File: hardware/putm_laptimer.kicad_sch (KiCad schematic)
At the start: 44 parts, among them J1 Conn_02x22_Top_Bottom, J10 Conn_01x07, J11 Conn_01x09, J12 Conn_01x01, J13 Conn_01x01, J14 Conn_01x01, J15 Conn_01x01, J16 2601-1103, J2 Conn_02x22_Top_Bottom, J5 2601-3109, J6 Conn_02x05_Odd_Even, J7 2601-1102, J8 2601-3109, J9 Conn_01x07

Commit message: Added part numbers
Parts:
- C1, C10, C3, C4, C5, C6, C7, C8, C9: Link (none) -> https://www.mouser.pl/ProductDetail/KYOCERA-AVX/06035A101KA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; Mouser Part Number (none) -> 581-06035A101K
- D1: Link (none) -> https://eu.mouser.com/ProductDetail/Diodes-Incorporated/DES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
- D2: Link (none) -> https://www.mouser.pl/ProductDetail/Diodes-Incorporated/MBR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
- J1, J2: Link (none) -> https://www.tme.eu/pl/details/zl262-50dg/listwy-i-gniazda-k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; Mouser Part Number (none) -> ZL262-50DG
- J10, J9: Link (none) -> https://www.tme.eu/pl/details/zl262-7sg/listwy-i-gniazda-ko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; Mouser Part Number (none) -> ZL262-7SG
- J11: Link (none) -> https://www.tme.eu/pl/details/zl262-9sg/listwy-i-gniazda-ko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; Mouser Part Number (none) -> ZL262-9SG
- J16, J5, J7, J8: Link (none) -> https://www.wago.com/pl/z%C5%82%C4%85czki-do-p%C5%82ytek-dr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
- J6: Link (none) -> https://www.tme.eu/pl/details/mx-70246-1004/zlacza-pozostal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; Mouser Part Number (none) -> MX-70246-1004
- R1, R11, R13, R15, R17, R19, R5, R7, R9: Link (none) -> https://www.mouser.pl/ProductDetail/Bourns/CR0603-FX-1001EL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; Mouser Part Number (none) -> 652-CR0603FX-1001ELF
- R10, R12, R14, R16, R18, R2, R20, R6, R8: Link (none) -> https://www.mouser.pl/ProductDetail/Bourns/CR0603-FX-1002EL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; Mouser Part Number (none) -> 652-CR0603FX-1002ELF
- R21: Link (none) -> https://www.mouser.pl/ProductDetail/Bourns/CR0603-FX-3300EL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; Mouser Part Number (none) -> 652-CR0603FX-3300ELF

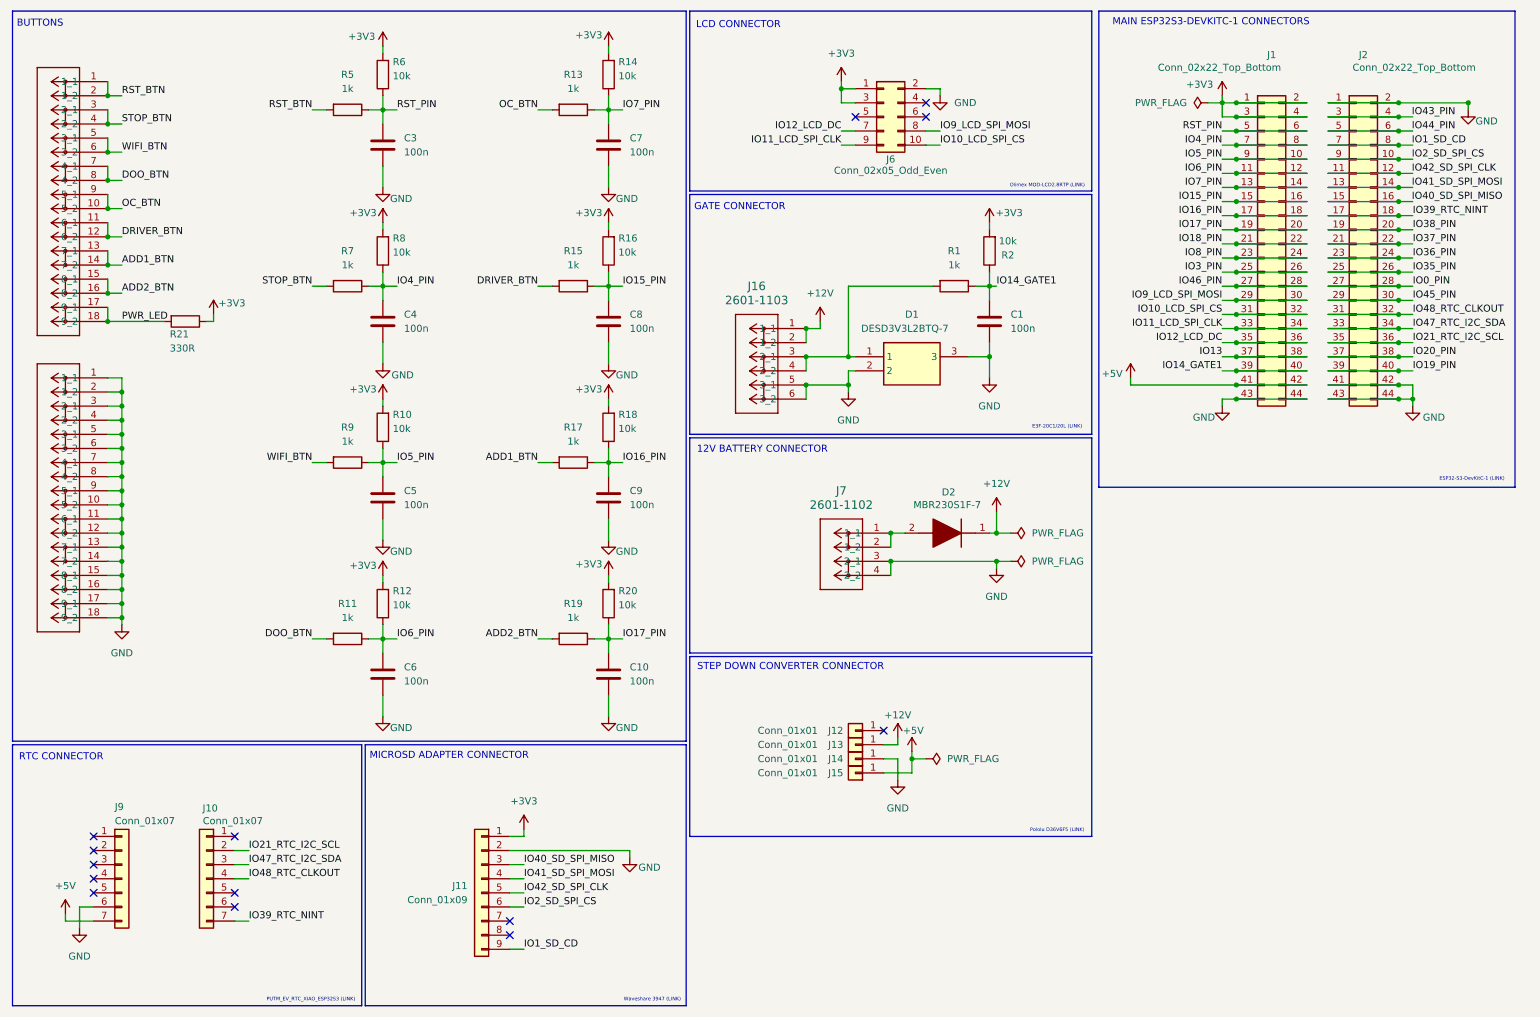
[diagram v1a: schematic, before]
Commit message: Fixed silkscreen text size
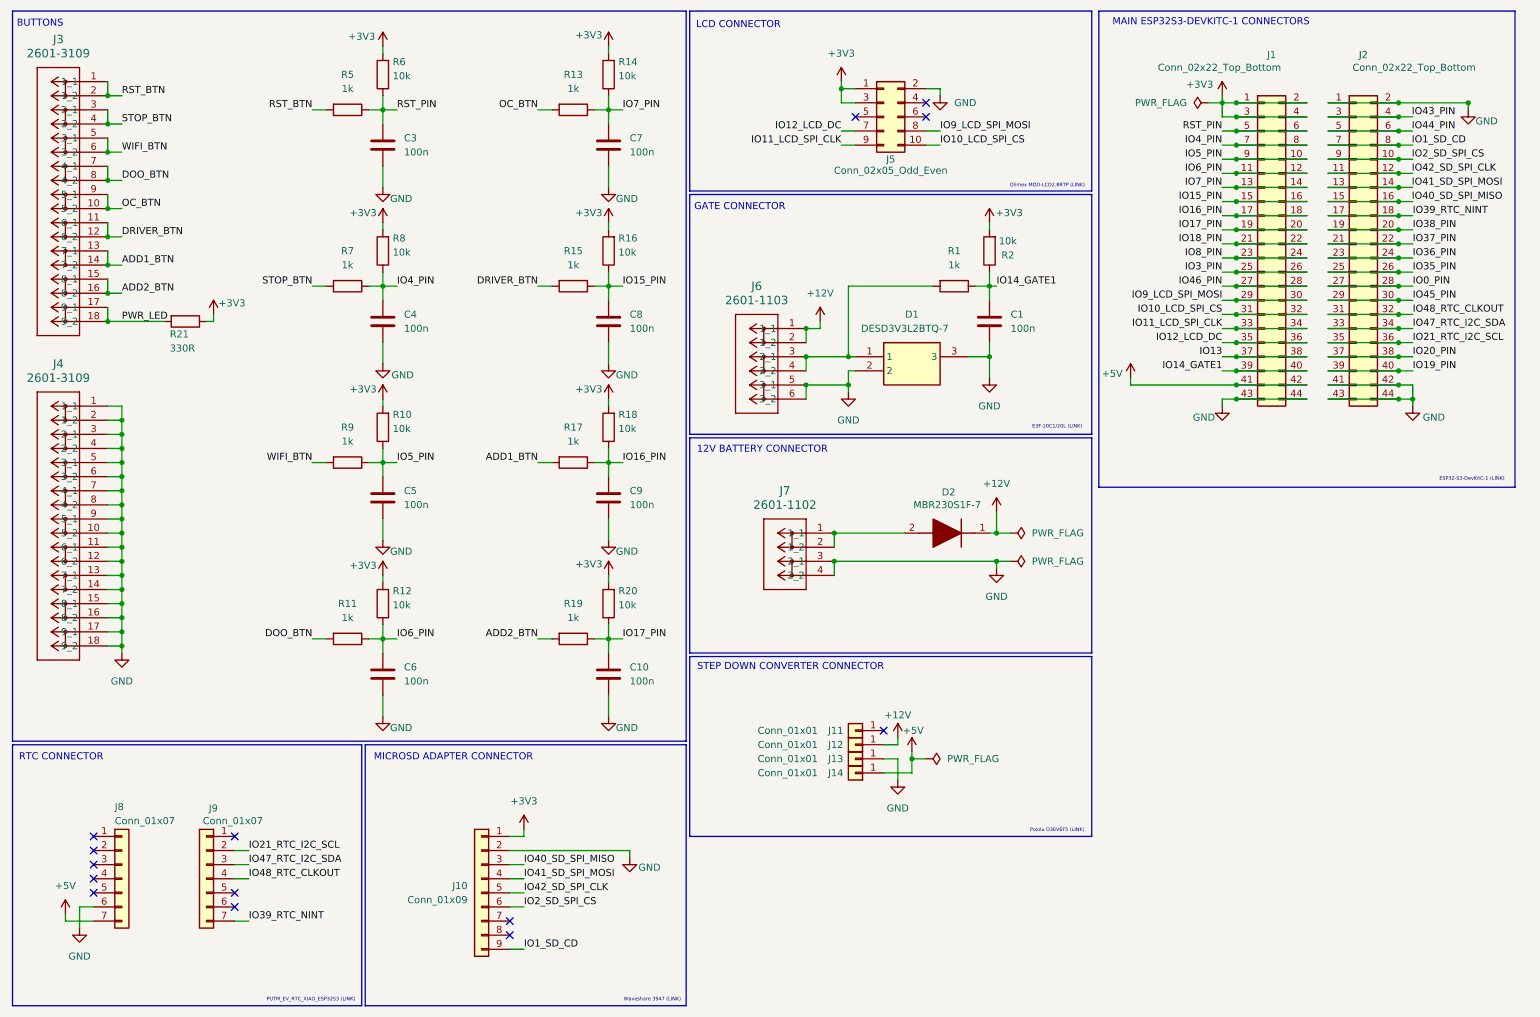
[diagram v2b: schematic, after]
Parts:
- renumbered J11 to J10, J12 to J11, J13 to J12, J14 to J13, J15 to J14, J8 to J3, J5 to J4, J6 to J5, J16 to J6, J9 to J8, J10 to J9
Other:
- moved on the sheet: J7

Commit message: Fixed connector placing
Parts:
- removed J1, J2: Conn_02x22_Top_Bottom, Connector_PinSocket_2.54mm:PinSocket_2x22_P2.54mm_Vertical, symbol Connector_Generic:Conn_02x22_Odd_Even
- added J1, J2, J3, J4: Conn_01x22, Connector_PinSocket_2.54mm:PinSocket_1x22_P2.54mm_Vertical, symbol Connector_Generic:Conn_01x22
- renumbered J8 to J10, J9 to J11, J10 to J12, J11 to J13, J12 to J14, J13 to J15, J14 to J16, J3 to J5, J4 to J6, J5 to J7, J6 to J8, J7 to J9
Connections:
- net +3V3: now also J1.1 (Pin_1), J1.2 (Pin_2), J3.1 (Pin_1), J3.2 (Pin_2)
- net +5V: now also J1.21 (Pin_21), J3.21 (Pin_21)
- net GND: now also J1.22 (Pin_22), J2.1 (Pin_1), J2.21 (Pin_21), J2.22 (Pin_22), J3.22 (Pin_22), J4.1 (Pin_1), J4.21 (Pin_21), J4.22 (Pin_22)
- net IO0_PIN: now also J2.14 (Pin_14), J4.14 (Pin_14)
- net IO10_LCD_SPI_CS: now also J1.16 (Pin_16), J3.16 (Pin_16)
- net IO11_LCD_SPI_CLK: now also J1.17 (Pin_17), J3.17 (Pin_17)
- net IO12_LCD_DC: now also J1.18 (Pin_18), J3.18 (Pin_18)
- net IO13: now also J1.19 (Pin_19), J3.19 (Pin_19)
- net IO14_GATE1: now also J1.20 (Pin_20), J3.20 (Pin_20)
- net IO15_PIN: now also J1.8 (Pin_8), J3.8 (Pin_8)
- net IO16_PIN: now also J1.9 (Pin_9), J3.9 (Pin_9)
- net IO17_PIN: now also J1.10 (Pin_10), J3.10 (Pin_10)
- net IO18_PIN: now also J1.11 (Pin_11), J3.11 (Pin_11)
- net IO19_PIN: now also J2.20 (Pin_20), J4.20 (Pin_20)
- net IO1_SD_CD: now also J2.4 (Pin_4), J4.4 (Pin_4)
- net IO20_PIN: now also J2.19 (Pin_19), J4.19 (Pin_19)
- net IO21_RTC_I2C_SCL: now also J2.18 (Pin_18), J4.18 (Pin_18)
- net IO2_SD_SPI_CS: now also J2.5 (Pin_5), J4.5 (Pin_5)
- net IO35_PIN: now also J2.13 (Pin_13), J4.13 (Pin_13)
- net IO36_PIN: now also J2.12 (Pin_12), J4.12 (Pin_12)
- net IO37_PIN: now also J2.11 (Pin_11), J4.11 (Pin_11)
- net IO38_PIN: now also J2.10 (Pin_10), J4.10 (Pin_10)
- net IO39_RTC_NINT: now also J2.9 (Pin_9), J4.9 (Pin_9)
- net IO3_PIN: now also J1.13 (Pin_13), J3.13 (Pin_13)
- net IO40_SD_SPI_MISO: now also J2.8 (Pin_8), J4.8 (Pin_8)
- net IO41_SD_SPI_MOSI: now also J2.7 (Pin_7), J4.7 (Pin_7)
- net IO42_SD_SPI_CLK: now also J2.6 (Pin_6), J4.6 (Pin_6)
- net IO43_PIN: now also J2.2 (Pin_2), J4.2 (Pin_2)
- net IO44_PIN: now also J2.3 (Pin_3), J4.3 (Pin_3)
- net IO45_PIN: now also J2.15 (Pin_15), J4.15 (Pin_15)
- net IO46_PIN: now also J1.14 (Pin_14), J3.14 (Pin_14)
- net IO47_RTC_I2C_SDA: now also J2.17 (Pin_17), J4.17 (Pin_17)
- net IO48_RTC_CLKOUT: now also J2.16 (Pin_16), J4.16 (Pin_16)
- net IO4_PIN: now also J1.4 (Pin_4), J3.4 (Pin_4)
- net IO5_PIN: now also J1.5 (Pin_5), J3.5 (Pin_5)
- net IO6_PIN: now also J1.6 (Pin_6), J3.6 (Pin_6)
- net IO7_PIN: now also J1.7 (Pin_7), J3.7 (Pin_7)
- net IO8_PIN: now also J1.12 (Pin_12), J3.12 (Pin_12)
- net IO9_LCD_SPI_MOSI: now also J1.15 (Pin_15), J3.15 (Pin_15)
- net RST_PIN: now also J1.3 (Pin_3), J3.3 (Pin_3)
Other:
- note added: "ADDITIONAL CONNECTORS"
- moved on the sheet: D2, J9

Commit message: Changed lcd connector model
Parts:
- J7: footprint Connector_PinHeader_2.54mm:PinHeader_2x05_P2.54mm_Vertical_SMD -> Connector_PinHeader_2.54mm:PinHeader_2x05_P2.54mm_Vertical; Link https://www.tme.eu/pl/details/mx-70246-1004/zlacza-pozostal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 -> https://www.tme.eu/pl/details/zl231-10pg/zlacza-idc/connfly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; Mouser Part Number MX-70246-1004 -> ZL231-10PG
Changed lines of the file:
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@@
 			)
 		)
-		(property "Footprint" "Connector_PinHeader_2.54mm:PinHeader_2x05_P2.54mm_Vertical_SMD"
+		(property "Footprint" "Connector_PinHeader_2.54mm:PinHeader_2x05_P2.54mm_Vertical"
 			(at 170.18 33.02 0)
 			(effects
@@
 			)
 		)
-		(property "Link" "https://www.tme.eu/pl/details/mx-70246-1004/zlacza-pozostale-molex/molex/70246-1004/?brutto=1&currency=PLN&utm_content=&campaign_id=20675111424&gad_campaignid=20675111424"
+		(property "Link" "https://www.tme.eu/pl/details/zl231-10pg/zlacza-idc/connfly/ds1013-10ssib1-b-0/"
 			(at 170.18 33.02 0)
 			(effects
@@
 			)
 		)
-		(property "Mouser Part Number" "MX-70246-1004"
+		(property "Mouser Part Number" "ZL231-10PG"
 			(at 170.18 33.02 0)
 			(effects

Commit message: Changed capactitor model
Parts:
- C1, C10, C3, C4, C5, C6, C7, C8, C9: Link https://www.mouser.pl/ProductDetail/KYOCERA-AVX/06035A101KA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 -> https://www.mouser.pl/ProductDetail/Murata-Electronics/GRM0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; Mouser Part Number 581-06035A101K -> 81-GRM33R6YA104ME14D
- D1: Link https://eu.mouser.com/ProductDetail/Diodes-Incorporated/DES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 -> https://www.mouser.pl/ProductDetail/Diodes-Incorporated/DES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
- J7: footprint Connector_PinHeader_2.54mm:PinHeader_2x05_P2.54mm_Vertical -> Connector_PinHeader_2.54mm:PinHeader_2x05_P2.54mm_Vertical_SMD; Link https://www.tme.eu/pl/details/zl231-10pg/zlacza-idc/connfly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 -> https://www.tme.eu/pl/details/mx-70246-1004/zlacza-pozostal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; Mouser Part Number ZL231-10PG -> MX-70246-1004
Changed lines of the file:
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@@
 			)
 		)
-		(property "Footprint" "Connector_PinHeader_2.54mm:PinHeader_2x05_P2.54mm_Vertical"
+		(property "Footprint" "Connector_PinHeader_2.54mm:PinHeader_2x05_P2.54mm_Vertical_SMD"
 			(at 170.18 33.02 0)
 			(effects
@@
 			)
 		)
-		(property "Link" "https://www.tme.eu/pl/details/zl231-10pg/zlacza-idc/connfly/ds1013-10ssib1-b-0/"
+		(property "Link" "https://www.tme.eu/pl/details/mx-70246-1004/zlacza-pozostale-molex/molex/70246-1004/?brutto=1&currency=PLN&utm_content=&campaign_id=20675111424&gad_campaignid=20675111424"
 			(at 170.18 33.02 0)
 			(effects
@@
 			)
 		)
-		(property "Mouser Part Number" "ZL231-10PG"
+		(property "Mouser Part Number" "MX-70246-1004"
 			(at 170.18 33.02 0)
 			(effects
@@
 			)
 		)
-		(property "Link" "https://www.mouser.pl/ProductDetail/KYOCERA-AVX/06035A101KAT2A?qs=I5rfTV0A4wHSVYt8pWypSg%3D%3D"
+		(property "Link" "https://www.mouser.pl/ProductDetail/Murata-Electronics/GRM033R6YA104ME14D?qs=P%2FC4Eoq9CDwjSVlAMBrT%252Bw%3D%3D"
 			(at 80.01 69.85 0)
 			(effects
@@
 			)
 		)
-		(property "Mouser Part Number" "581-06035A101K "
+		(property "Mouser Part Number" "81-GRM33R6YA104ME14D "
 			(at 80.01 69.85 0)
 			(effects
@@
 			)
 		)
-		(property "Link" "https://www.mouser.pl/ProductDetail/KYOCERA-AVX/06035A101KAT2A?qs=I5rfTV0A4wHSVYt8pWypSg%3D%3D"
+		(property "Link" "https://www.mouser.pl/ProductDetail/Murata-Electronics/GRM033R6YA104ME14D?qs=P%2FC4Eoq9CDwjSVlAMBrT%252Bw%3D%3D"
 			(at 80.01 38.1 0)
 			(effects
@@
 			)
 		)
-		(property "Mouser Part Number" "581-06035A101K "
+		(property "Mouser Part Number" "81-GRM33R6YA104ME14D "
 			(at 80.01 38.1 0)
 			(effects
@@
 			)
 		)
-		(property "Link" "https://www.mouser.pl/ProductDetail/KYOCERA-AVX/06035A101KAT2A?qs=I5rfTV0A4wHSVYt8pWypSg%3D%3D"
+		(property "Link" "https://www.mouser.pl/ProductDetail/Murata-Electronics/GRM033R6YA104ME14D?qs=P%2FC4Eoq9CDwjSVlAMBrT%252Bw%3D%3D"
 			(at 120.65 101.6 0)
 			(effects
@@
 			)
 		)
-		(property "Mouser Part Number" "581-06035A101K "
+		(property "Mouser Part Number" "81-GRM33R6YA104ME14D "
 			(at 120.65 101.6 0)
 			(effects
@@
 			)
 		)
-		(property "Link" "https://www.mouser.pl/ProductDetail/KYOCERA-AVX/06035A101KAT2A?qs=I5rfTV0A4wHSVYt8pWypSg%3D%3D"
+		(property "Link" "https://www.mouser.pl/ProductDetail/Murata-Electronics/GRM033R6YA104ME14D?qs=P%2FC4Eoq9CDwjSVlAMBrT%252Bw%3D%3D"
 			(at 120.65 38.1 0)
 			(effects
@@
 			)
 		)
-		(property "Mouser Part Number" "581-06035A101K "
+		(property "Mouser Part Number" "81-GRM33R6YA104ME14D "
 			(at 120.65 38.1 0)
 			(effects
@@
 			)
 		)
-		(property "Link" "https://www.mouser.pl/ProductDetail/KYOCERA-AVX/06035A101KAT2A?qs=I5rfTV0A4wHSVYt8pWypSg%3D%3D"
+		(property "Link" "https://www.mouser.pl/ProductDetail/Murata-Electronics/GRM033R6YA104ME14D?qs=P%2FC4Eoq9CDwjSVlAMBrT%252Bw%3D%3D"
 			(at 80.01 101.6 0)
 			(effects
@@
 			)
 		)
-		(property "Mouser Part Number" "581-06035A101K "
+		(property "Mouser Part Number" "81-GRM33R6YA104ME14D "
 			(at 80.01 101.6 0)
 			(effects
@@
 			)
 		)
-		(property "Link" "https://www.mouser.pl/ProductDetail/KYOCERA-AVX/06035A101KAT2A?qs=I5rfTV0A4wHSVYt8pWypSg%3D%3D"
+		(property "Link" "https://www.mouser.pl/ProductDetail/Murata-Electronics/GRM033R6YA104ME14D?qs=P%2FC4Eoq9CDwjSVlAMBrT%252Bw%3D%3D"
 			(at 80.01 133.35 0)
 			(effects
@@
 			)
 		)
-		(property "Mouser Part Number" "581-06035A101K "
+		(property "Mouser Part Number" "81-GRM33R6YA104ME14D "
 			(at 80.01 133.35 0)
 			(effects
@@
 			)
 		)
-		(property "Link" "https://www.mouser.pl/ProductDetail/KYOCERA-AVX/06035A101KAT2A?qs=I5rfTV0A4wHSVYt8pWypSg%3D%3D"
+		(property "Link" "https://www.mouser.pl/ProductDetail/Murata-Electronics/GRM033R6YA104ME14D?qs=P%2FC4Eoq9CDwjSVlAMBrT%252Bw%3D%3D"
 			(at 120.65 69.85 0)
 			(effects
@@
 			)
 		)
-		(property "Mouser Part Number" "581-06035A101K "
+		(property "Mouser Part Number" "81-GRM33R6YA104ME14D "
 			(at 120.65 69.85 0)
 			(effects
@@
 			)
 		)
-		(property "Link" "https://www.mouser.pl/ProductDetail/KYOCERA-AVX/06035A101KAT2A?qs=I5rfTV0A4wHSVYt8pWypSg%3D%3D"
+		(property "Link" "https://www.mouser.pl/ProductDetail/Murata-Electronics/GRM033R6YA104ME14D?qs=P%2FC4Eoq9CDwjSVlAMBrT%252Bw%3D%3D"
 			(at 120.65 133.35 0)
 			(effects
@@
 			)
 		)
-		(property "Mouser Part Number" "581-06035A101K "
+		(property "Mouser Part Number" "81-GRM33R6YA104ME14D "
 			(at 120.65 133.35 0)
 			(effects
@@
 			)
 		)
-		(property "Link" "https://www.mouser.pl/ProductDetail/KYOCERA-AVX/06035A101KAT2A?qs=I5rfTV0A4wHSVYt8pWypSg%3D%3D"
+		(property "Link" "https://www.mouser.pl/ProductDetail/Murata-Electronics/GRM033R6YA104ME14D?qs=P%2FC4Eoq9CDwjSVlAMBrT%252Bw%3D%3D"
 			(at 189.23 69.85 0)
 			(effects
@@
 			)
 		)
-		(property "Mouser Part Number" "581-06035A101K "
+		(property "Mouser Part Number" "81-GRM33R6YA104ME14D "
 			(at 189.23 69.85 0)
 			(effects
@@
 			)
 		)
-		(property "Link" "https://eu.mouser.com/ProductDetail/Diodes-Incorporated/DESD3V3L2BTQ-7?qs=QNEnbhJQKvaDjKgdozA%2FQw%3D%3D"
+		(property "Link" "https://www.mouser.pl/ProductDetail/Diodes-Incorporated/DESD3V3L2BTQ-7?qs=QNEnbhJQKvaDjKgdozA%2FQw%3D%3D&_gl=1*1bh7tjn*_ga*dW5kZWZpbmVk*_ga_15W4STQT4T*dW5kZWZpbmVk*_ga_1KQLCYKRX3*dW5kZWZpbmVk"
 			(at 165.1 76.2 0)
 			(effects
